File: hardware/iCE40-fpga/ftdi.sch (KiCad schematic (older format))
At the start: 17 parts, among them U7 93C46B, U8 FT2232H

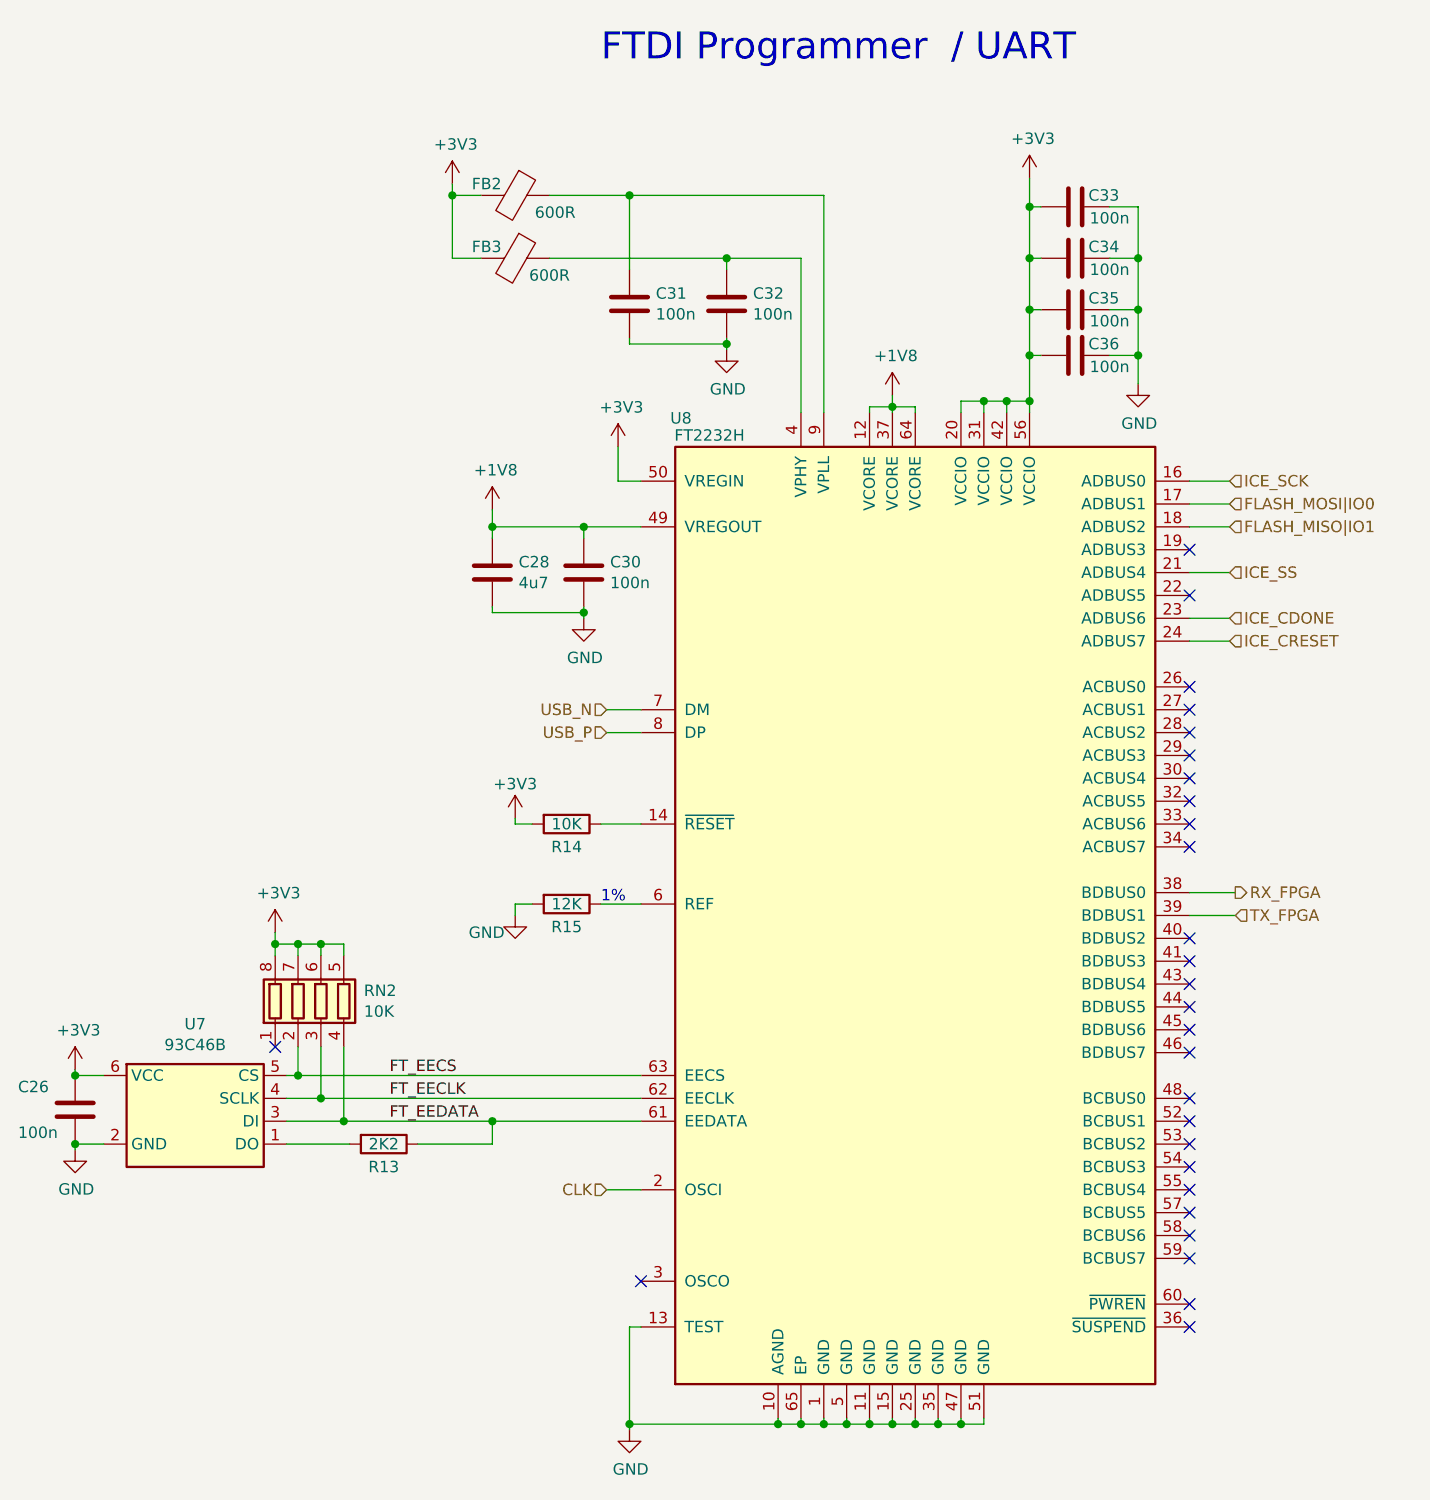
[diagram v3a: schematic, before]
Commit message: changes to make everything work with new library setup
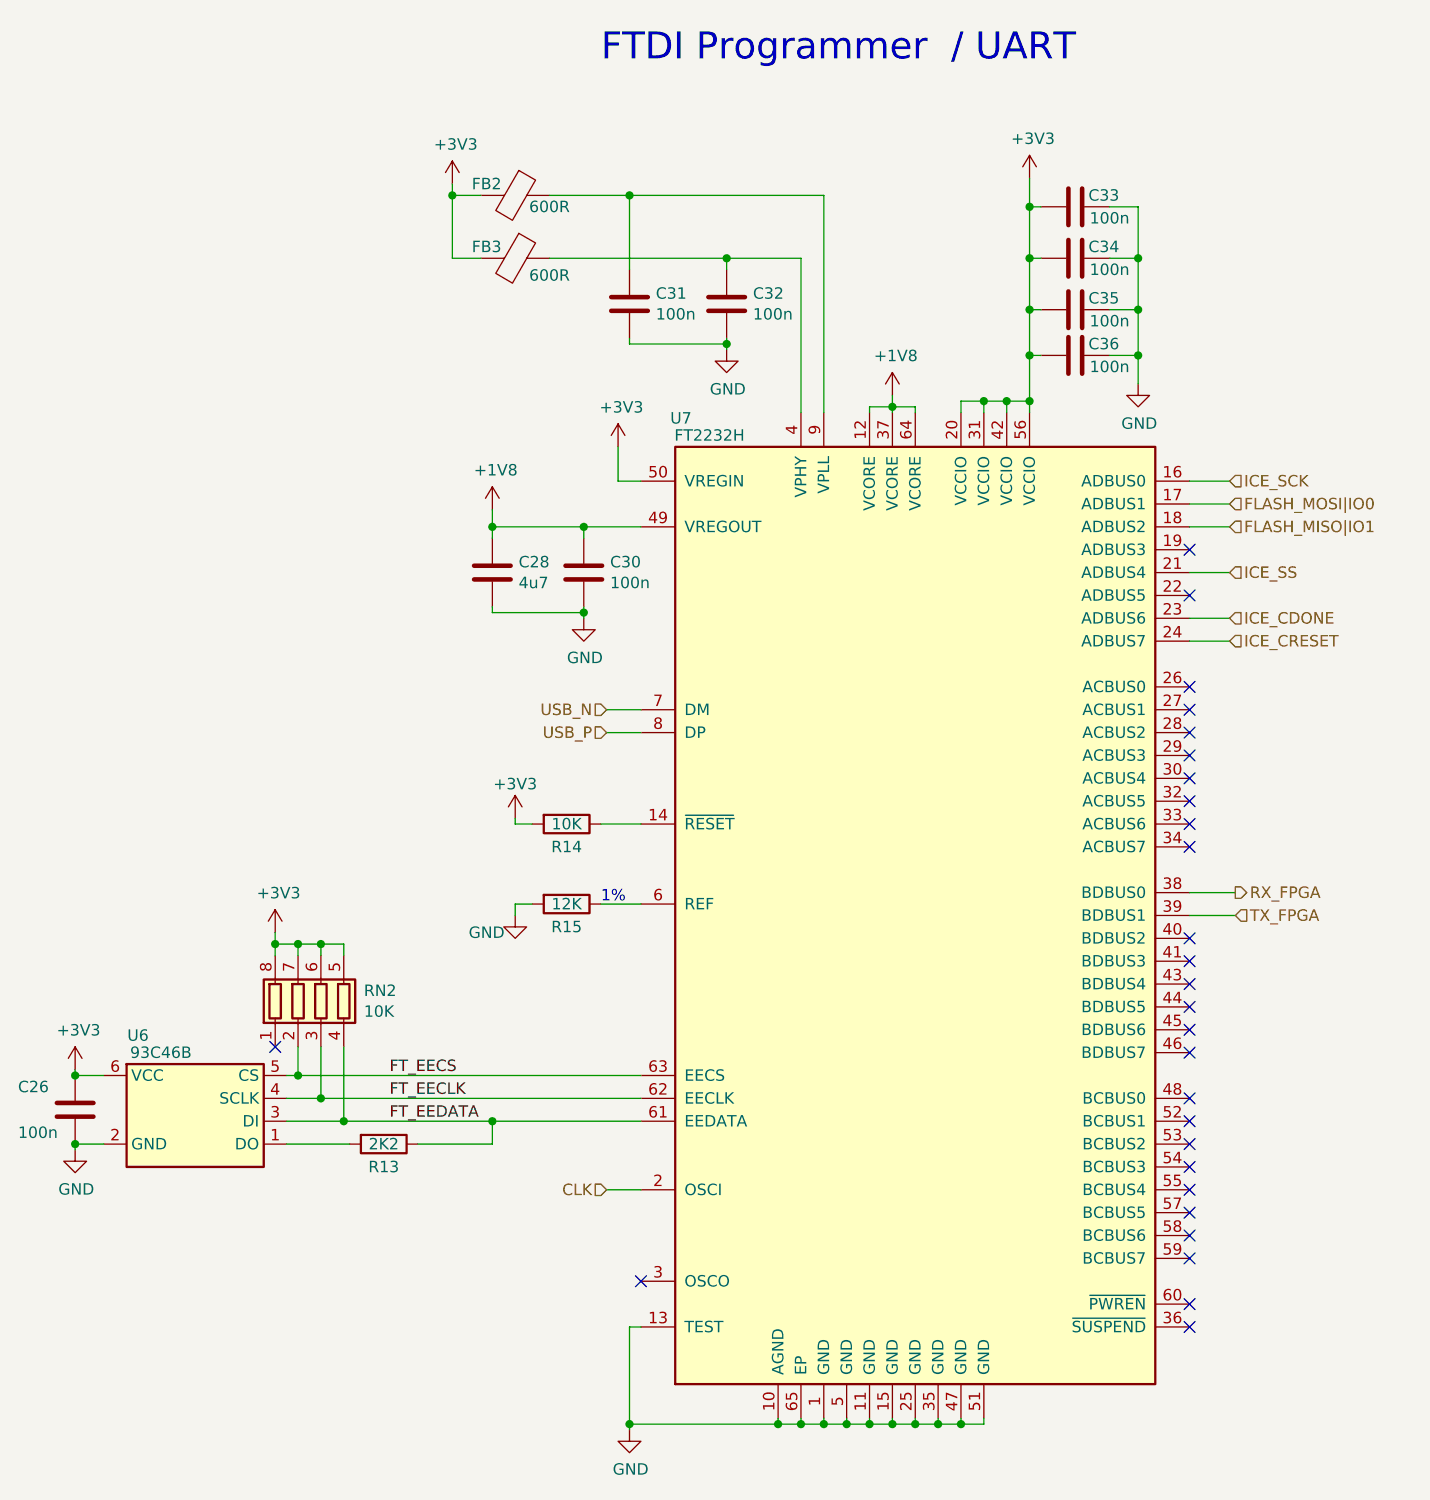
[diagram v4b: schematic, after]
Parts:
- removed FB2, FB3: 600R, josh-footprints:BEADC1608X95N, symbol josh-symbols:Ferrite_Bead_PWR
- removed U7: 93C46B, Package_TO_SOT_SMD:SOT-23-6, symbol josh-symbols:93C46B
- removed U8: FT2232H, josh-footprints:QFN-64-1EP_9x9mm_P0.5mm_EP4.7x4.7mm_ThermalVias, symbol josh-symbols:FT2232H
- added FB2, FB3: 600R, josh-passives-smt:Ferrite_Bead_0603, symbol josh-passive:Ferrite_Bead_PWR
- added U6: 93C46B, Package_TO_SOT_SMD:SOT-23-6, symbol josh-memory:93C46B
- added U7: FT2232H, josh-dfn-qfn:QFN-64-1EP_9x9mm_P0.5mm_EP4.7x4.7mm_ThermalVias, symbol josh-ic:FT2232H
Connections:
- net +1V8: now also U7.12 (VCORE), U7.37 (VCORE), U7.49 (VREGOUT), U7.64 (VCORE)
- net +3V3: now also FB2.2, FB3.2, U6.6 (VCC), U7.20 (VCCIO), U7.31 (VCCIO), U7.42 (VCCIO), U7.50 (VREGIN), U7.56 (VCCIO)
- net CLK: now also U7.2 (OSCI)
- net FLASH_MISO|IO1: now also U7.18 (ADBUS2)
- net FLASH_MOSI|IO0: now also U7.17 (ADBUS1)
- net FT_EECLK: now also U6.4 (SCLK), U7.62 (EECLK)
- net FT_EECS: now also U6.5 (CS), U7.63 (EECS)
- net FT_EEDATA: now also U6.3 (DI), U7.61 (EEDATA)
- net GND: now also U6.2 (GND), U7.1 (GND), U7.10 (AGND), U7.11 (GND), U7.13 (TEST), U7.15 (GND), U7.25 (GND), U7.35 (GND), U7.47 (GND), U7.5 (GND), U7.51 (GND), U7.65 (EP)
- net ICE_CDONE: now also U7.23 (ADBUS6)
- net ICE_CRESET: now also U7.24 (ADBUS7)
- net ICE_SCK: now also U7.16 (ADBUS0)
- net ICE_SS: now also U7.21 (ADBUS4)
- net RX_FPGA: now also U7.38 (BDBUS0)
- net TX_FPGA: now also U7.39 (BDBUS1)
- net USB_N: now also U7.7 (DM)
- net USB_P: now also U7.8 (DP)
- net at R13.2: now also U6.1 (DO)
- net at R14.1: now also U7.14 (~RESET)
- net at R15.1: now also U7.6 (REF)
- net at C31.1: now also FB2.1, U7.9 (VPLL)
- net at C32.1: now also FB3.1, U7.4 (VPHY)
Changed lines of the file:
@@
 	3975 6900 4625 6900
 Connection ~ 3375 5575
-$Comp
-L josh-symbols:FT2232H U8
-U 1 1 60207C83
-P 5225 4675
-F 0 "U8" H 4200 6850 50  0000 C CNN
-F 1 "FT2232H" H 4325 6775 50  0000 C CNN
-F 2 "josh-footprints:QFN-64-1EP_9x9mm_P0.5mm_EP4.7x4.7mm_ThermalVias" H 5225 4675 50  0001 C CNN
-F 3 "http://www.ftdichip.com/Products/ICs/FT2232H.html" H 5225 4675 50  0001 C CNN
-	1    5225 4675
-	1    0    0    -1
-$EndComp
 Text HLabel 3875 3775 0    50   Input ~ 0
 USB_N
@@
 Wire Wire Line
 	3325 1800 3200 1800
-$Comp
-L josh-symbols:Ferrite_Bead_PWR FB?
-U 1 1 5EDD47E7
-P 3475 1800
-AR Path="/5EDD47E7" Ref="FB?"  Part="1"
-AR Path="/5ED7AB6B/5EDD47E7" Ref="FB3"  Part="1"
-F 0 "FB3" V 3425 1675 50  0000 C CNN
-F 1 "600R " V 3550 1950 50  0000 C CNN
-F 2 "josh-footprints:BEADC1608X95N" V 3405 1800 50  0001 C CNN
-F 3 "~" H 3475 1800 50  0001 C CNN
-	1    3475 1800
-	0    1    1    0
-$EndComp
-$Comp
-L josh-symbols:Ferrite_Bead_PWR FB?
-U 1 1 5EDD47E1
-P 3475 1525
-AR Path="/5EDD47E1" Ref="FB?"  Part="1"
-AR Path="/5ED7AB6B/5EDD47E1" Ref="FB2"  Part="1"
-F 0 "FB2" V 3425 1400 50  0000 C CNN
-F 1 "600R " V 3550 1700 50  0000 C CNN
-F 2 "josh-footprints:BEADC1608X95N" V 3405 1525 50  0001 C CNN
-F 3 "~" H 3475 1525 50  0001 C CNN
-	1    3475 1525
-	0    1    1    0
-$EndComp
 Wire Wire Line
 	3200 1525 3325 1525
@@
 NoConn ~ 6425 6375
 NoConn ~ 6425 6475
-$Comp
-L josh-symbols:93C46B U7
-U 1 1 61FB4482
-P 2075 5575
-F 0 "U7" H 2075 6000 50  0000 C CNN
-F 1 "93C46B" H 2075 5909 50  0000 C CNN
-F 2 "Package_TO_SOT_SMD:SOT-23-6" H 2075 5575 50  0001 C CNN
-F 3 "http://ww1.microchip.com/downloads/en/DeviceDoc/20001749K.pdf" H 2075 5575 50  0001 C CNN
-	1    2075 5575
-	1    0    0    -1
-$EndComp
 Wire Wire Line
 	3625 1800 4400 1800
@@
 Wire Wire Line
 	4725 6900 4825 6900
+$Comp
+L josh-memory:93C46B U6
+U 1 1 5D14D3ED
+P 2075 5525
+F 0 "U6" H 2325 5850 50  0000 C CNN
+F 1 "93C46B" H 2225 5775 50  0000 C CNN
+F 2 "Package_TO_SOT_SMD:SOT-23-6" H 2075 5475 50  0001 C CNN
+F 3 "http://ww1.microchip.com/downloads/en/DeviceDoc/20001749K.pdf" H 2075 5475 50  0001 C CNN
+	1    2075 5525
+	-1   0    0    -1
+$EndComp
+$Comp
+L josh-ic:FT2232H U7
+U 1 1 5D152328
+P 5225 4675
+F 0 "U7" H 4200 6850 50  0000 C CNN
+F 1 "FT2232H" H 4325 6775 50  0000 C CNN
+F 2 "josh-dfn-qfn:QFN-64-1EP_9x9mm_P0.5mm_EP4.7x4.7mm_ThermalVias" H 5225 4675 50  0001 C CNN
+F 3 "" H 5225 4675 50  0001 C CNN
+	1    5225 4675
+	1    0    0    -1
+$EndComp
+$Comp
+L josh-passive:Ferrite_Bead_PWR FB2
+U 1 1 5D1534FB
+P 3475 1525
+F 0 "FB2" H 3600 1475 50  0000 C CNN
+F 1 "600R" H 3325 1575 50  0000 C CNN
+F 2 "josh-passives-smt:Ferrite_Bead_0603" H 3475 1455 50  0001 C CNN
+F 3 "~" V 3475 1525 50  0001 C CNN
+	1    3475 1525
+	-1   0    0    1
+$EndComp
+$Comp
+L josh-passive:Ferrite_Bead_PWR FB3
+U 1 1 5D153B32
+P 3475 1800
+F 0 "FB3" H 3600 1750 50  0000 C CNN
+F 1 "600R" H 3325 1875 50  0000 C CNN
+F 2 "josh-passives-smt:Ferrite_Bead_0603" H 3475 1730 50  0001 C CNN
+F 3 "~" V 3475 1800 50  0001 C CNN
+	1    3475 1800
+	-1   0    0    1
+$EndComp
 $EndSCHEMATC
